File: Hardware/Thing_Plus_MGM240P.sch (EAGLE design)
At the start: 99 parts, among them J1 THING_PLUS_LOGICAL, J2 USB Female Type C Connector, J3 QWIIC_RIGHT_ANGLE, J5 MICRO-SDFRICTION, Q1 20V/4.2A/52mΩ/1.4W, U1 MGM240P, U2 XC6222B331MR-G, U3 EFM32GG12B410F1024GL120, U4 MCP73831, U5 MAX17048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

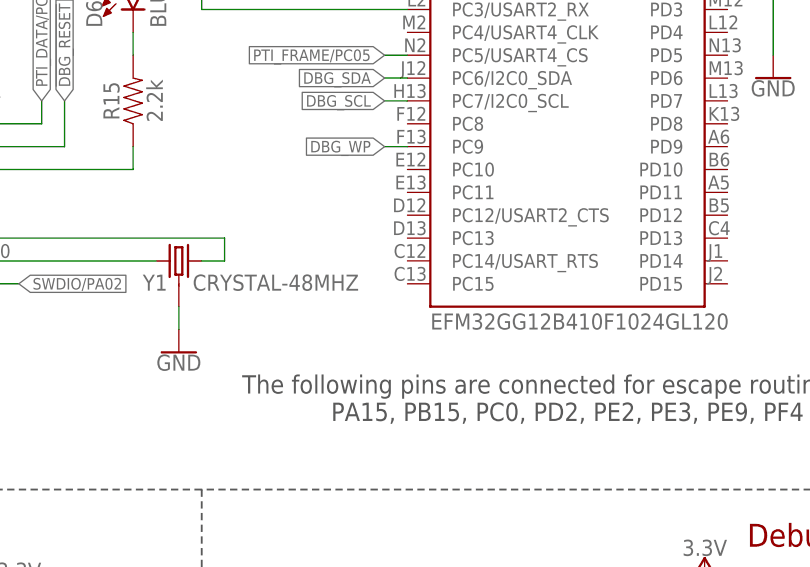
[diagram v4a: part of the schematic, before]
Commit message: Remove library files
Parts are in SFE Eagle library, update parts in design
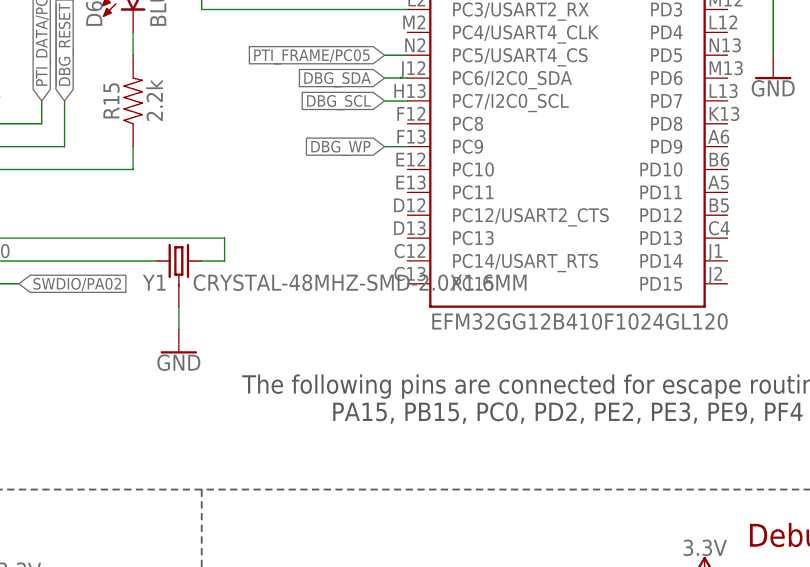
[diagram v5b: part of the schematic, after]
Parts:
- U1: device MGM240P:MGM240P -> SparkFun-RF:MGM240P
- U3: device EFM32GG12B410F1024GL120:EFM32GG12B410F1024GL120 -> SparkFun-IC-Microcontroller:EFM32GG12B410F1024GL120
- U6: device M24C02-FMC6TG:M24C02-FMC6TG -> SparkFun-IC-Memory:M24C02-FMC6TG
- U7: device MX25R8035FZUIL0:MX25R8035FZUIL0 -> SparkFun-IC-Memory:MX25R8035FZUIL0
- Y1: value CRYSTAL-48MHZ -> CRYSTAL-48MHZ-SMD-2.0X1.6MM; device CRYSTAL-48MHZ:CRYSTAL-48MHZ -> SparkFun-Clocks:CRYSTAL-48MHZ-SMD-2.0X1.6MM
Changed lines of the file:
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@@
 </classes>
 <parts>
-<part name="U1" library="MGM240P" deviceset="MGM240P" device=""/>
+<part name="U1" library="SparkFun-RF" deviceset="MGM240P" device=""/>
 <part name="J1" library="SparkFun-Boards" deviceset="THING_PLUS_LOGICAL" device=""/>
 <part name="FD1" library="SparkFun-Aesthetics" deviceset="FIDUCIAL" device="1X2"/>
@@
 <part name="SUPPLY31" library="SparkFun-PowerSymbols" deviceset="3.3V" device=""/>
 <part name="GND21" library="SparkFun-PowerSymbols" deviceset="GND" device=""/>
-<part name="U3" library="EFM32GG12B410F1024GL120" deviceset="EFM32GG12B410F1024GL120" device=""/>
+<part name="U3" library="SparkFun-IC-Microcontroller" deviceset="EFM32GG12" device="B410F1024GL120"/>
 <part name="TP1" library="SparkFun-Connectors" deviceset="TEST-POINT" device="3"/>
 <part name="TP2" library="SparkFun-Connectors" deviceset="TEST-POINT" device="3"/>
@@
 <part name="TP13" library="SparkFun-Connectors" deviceset="TEST-POINT" device="3"/>
 <part name="TP14" library="SparkFun-Connectors" deviceset="TEST-POINT" device="3"/>
-<part name="U6" library="M24C02-FMC6TG" deviceset="M24C02-FMC6TG" device=""/>
+<part name="U6" library="SparkFun-IC-Memory" deviceset="M24C02" device="-FMC6TG"/>
 <part name="GND14" library="SparkFun-PowerSymbols" deviceset="GND" device=""/>
 <part name="GND15" library="SparkFun-PowerSymbols" deviceset="GND" device=""/>
@@
 <part name="GND44" library="SparkFun-PowerSymbols" deviceset="GND" device=""/>
 <part name="GND45" library="SparkFun-PowerSymbols" deviceset="GND" device=""/>
-<part name="U7" library="MX25R8035FZUIL0" deviceset="MX25R8035FZUIL0" device=""/>
+<part name="U7" library="SparkFun-IC-Memory" deviceset="MX25R8035F" device="ZUIL0"/>
 <part name="R12" library="SparkFun-Resistors" deviceset="2.2KOHM" device="-0402T-1/16W-1%" value="2.2k"/>
 <part name="R16" library="SparkFun-Resistors" deviceset="2.2KOHM" device="-0402T-1/16W-1%" value="2.2k"/>
@@
 <part name="C21" library="SparkFun-Capacitors" deviceset="0.1UF" device="-0402T-6.3V-10%-X7R" value="0.1uF"/>
 <part name="GND48" library="SparkFun-PowerSymbols" deviceset="GND" device=""/>
-<part name="Y1" library="CRYSTAL-48MHZ" deviceset="CRYSTAL-48MHZ" device=""/>
+<part name="Y1" library="SparkFun-Clocks" deviceset="CRYSTAL-48MHZ" device="-SMD-2.0X1.6MM"/>
 <part name="GND49" library="SparkFun-PowerSymbols" deviceset="GND" device=""/>
 <part name="D8" library="SparkFun-DiscreteSemi" deviceset="DIODE-SCHOTTKY" device="-RB751S40" value="120mA/40V/370mV"/>
